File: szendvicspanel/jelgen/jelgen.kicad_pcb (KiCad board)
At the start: 2 copper layers, 100 x 45.5 mm, 24 parts, among them J1 Conn_01x04_Pin, U1 TL072, U2 TL072

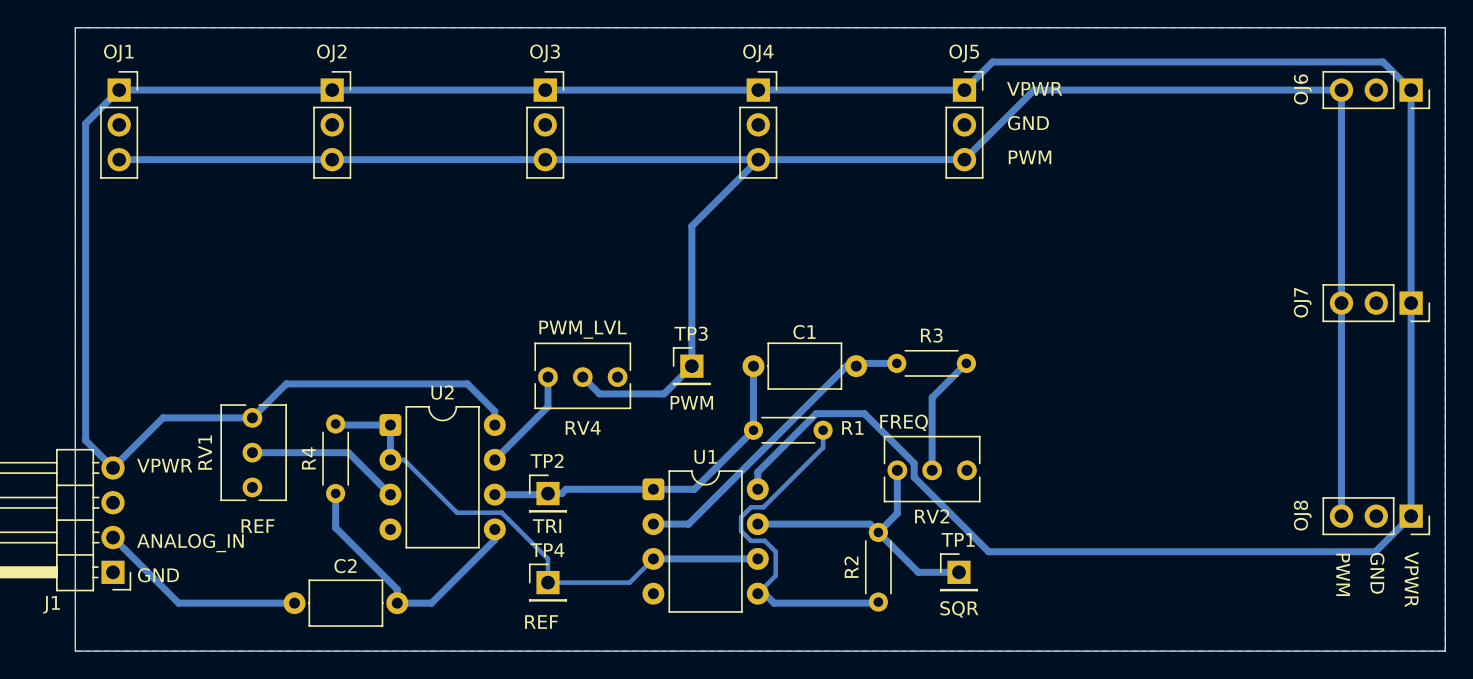
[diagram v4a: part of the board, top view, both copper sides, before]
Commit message: Analóg jelgen fix WIP
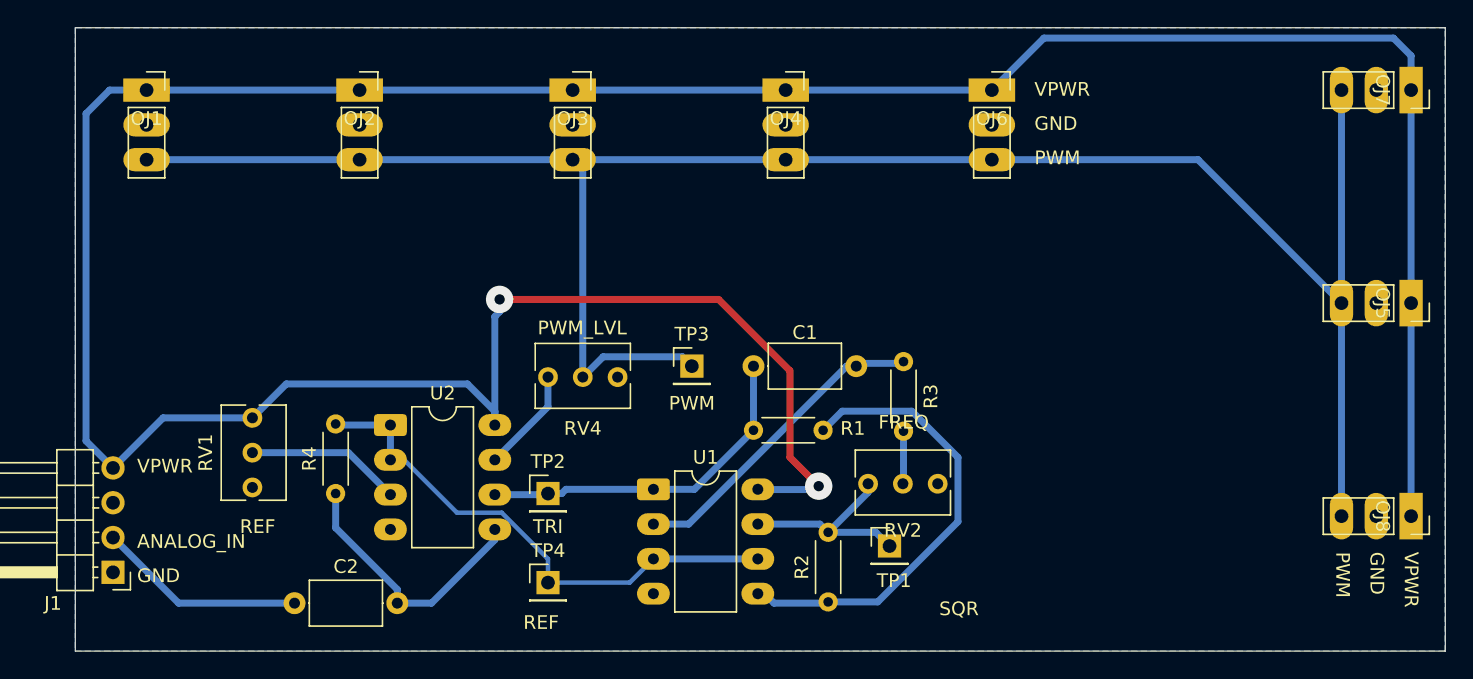
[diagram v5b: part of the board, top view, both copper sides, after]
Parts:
- OJ1, OJ2, OJ3, OJ4, OJ8: footprint Connector_PinSocket_2.54mm:PinSocket_1x03_P2.54mm_Vertical -> sajat:sajat_pin3
- OJ5: renamed from OJ7; footprint Connector_PinSocket_2.54mm:PinSocket_1x03_P2.54mm_Vertical -> sajat:sajat_pin3
- OJ6: renamed from OJ5; footprint Connector_PinSocket_2.54mm:PinSocket_1x03_P2.54mm_Vertical -> sajat:sajat_pin3
- OJ7: renamed from OJ6; footprint Connector_PinSocket_2.54mm:PinSocket_1x03_P2.54mm_Vertical -> sajat:sajat_pin3
- U1, U2: footprint Package_DIP:DIP-8_W7.62mm -> Package_DIP:DIP-8_W7.62mm_LongPads
- moved R3 6.75 mm to (138.4, 62.5), turned to 90 degrees
- moved TP1 5.42 mm to (137.4, 70.8)
- moved R2 3.67 mm to (132.9, 74.9)
- moved RV2 2.35 mm to (135.9, 66.3)
- moved OJ1 2.00 mm to (83.2, 37.5)
- moved OJ2 2.00 mm to (98.8, 37.5)
- moved OJ3 2.00 mm to (114.3, 37.5)
- moved OJ4 2.00 mm to (129.8, 37.5)
- moved OJ6 2.00 mm to (144.9, 37.5)
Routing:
- net Net-(U1B-+): track 26.2 -> 33.9 mm
- net VPWR: track 245.3 -> 238.6 mm, vias 0 -> 2
- net /SQUARE: track 21.3 -> 15.0 mm
- net Net-(R3-Pad1): track 8.84 -> 3.85 mm
- net /PWM: track 148.8 -> 147.7 mm

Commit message: Analóg jelgen fix
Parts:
- moved R2 0.72 mm to (133.3, 74.3)
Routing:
- net GND: track 0.00 -> 46.8 mm, vias 0 -> 2
- net VPWR: track 238.6 -> 221.8 mm
- net /REF: track 39.3 -> 44.3 mm, vias 0 -> 2
- net Net-(RV4-Pad1): track 7.65 -> 11.7 mm
- net Net-(U2B-+): track 19.7 -> 20.5 mm
- net /SQUARE: track 15.0 -> 14.3 mm
- net Net-(U1B-+): track 33.9 -> 33.3 mm
